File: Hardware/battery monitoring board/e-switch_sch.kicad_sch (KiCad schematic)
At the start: 8 parts, among them Q2 NMOS, Q3 PMOS, Q4 PMOS

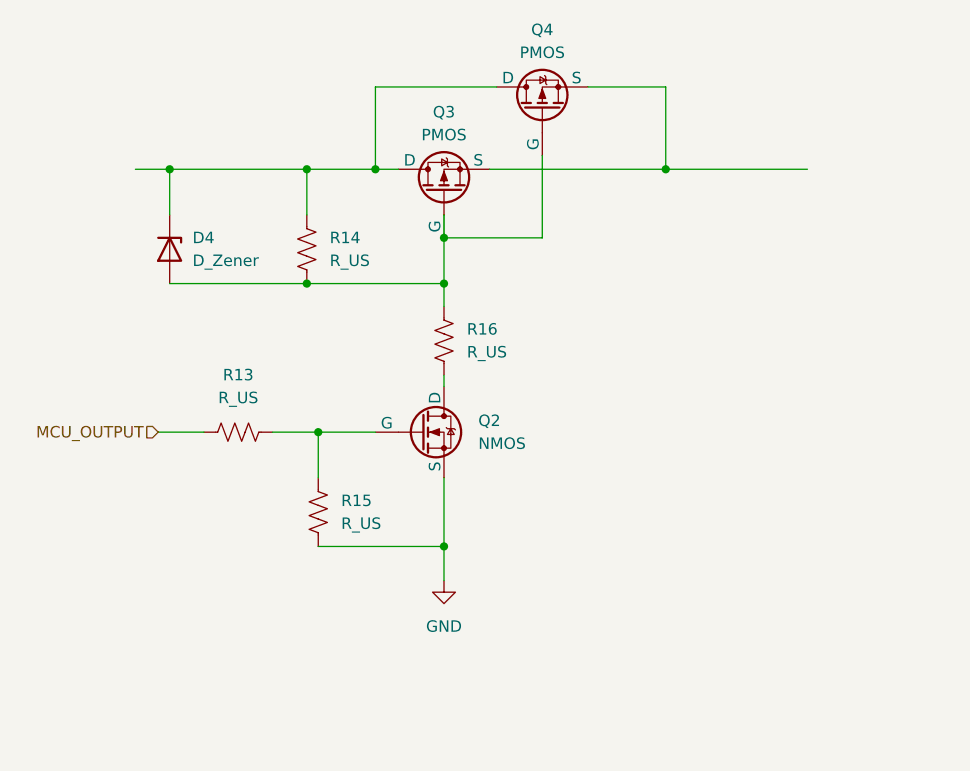
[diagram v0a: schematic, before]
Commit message: Added relay circuit
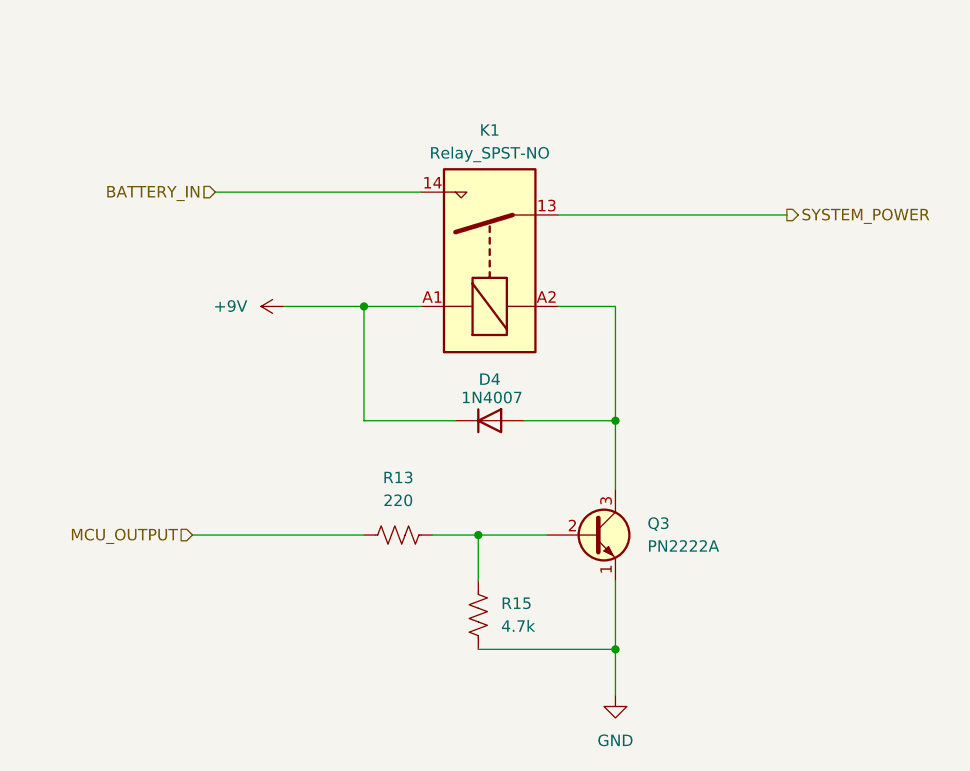
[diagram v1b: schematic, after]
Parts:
- removed D4: D_Zener, symbol Device:D_Zener
- removed Q2: NMOS, symbol Simulation_SPICE:NMOS
- removed Q3, Q4: PMOS, symbol Simulation_SPICE:PMOS
- removed R14, R16: R_US, symbol Device:R_US
- added D4: 1N4007, symbol Device:D
- added K1: Relay_SPST-NO, symbol Relay:Relay_SPST-NO
- added Q3: PN2222A, Package_TO_SOT_THT_AKL:TO-92_Inline_Wide_EBC, symbol PCM_Transistor_BJT_AKL:PN2222A
- R13: value R_US -> 220
- R15: value R_US -> 4.7k
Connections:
- net GND: now also Q3.1 (E)
- net at R13.2, R15.1: now also Q3.2 (B)
- new net: D4.2 (A), K1.A2, Q3.3 (C)
- new net +9V: D4.1 (K), K1.A1
- new net BATTERY_IN: K1.14
- new net SYSTEM_POWER: K1.13
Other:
- moved on the sheet: R13, R15

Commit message: Updated reference labels
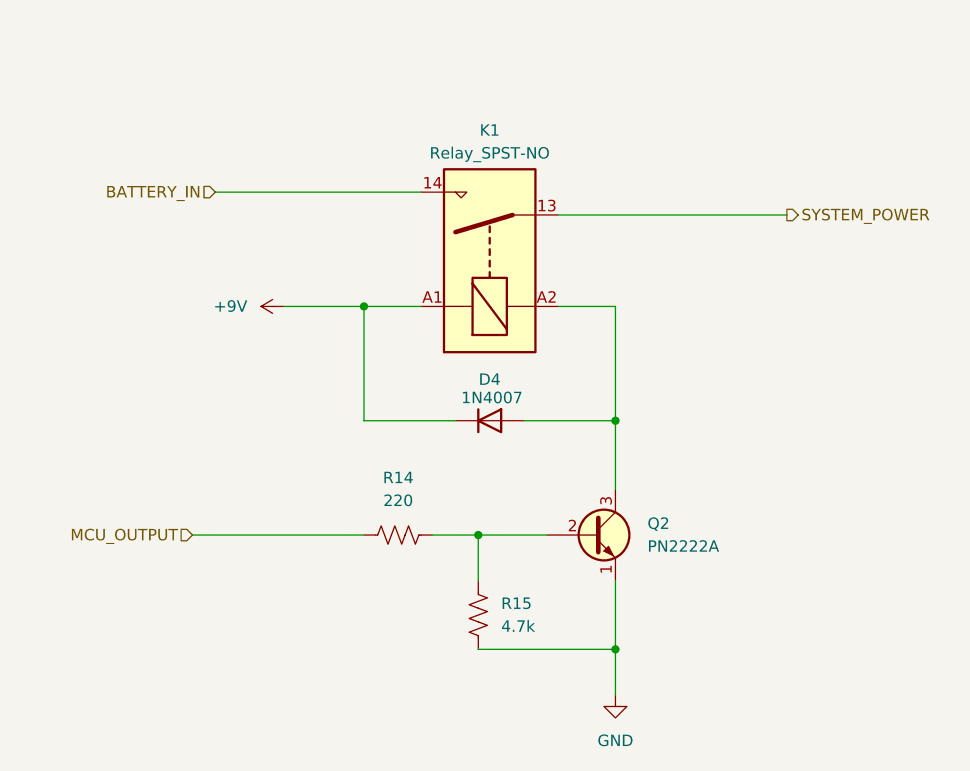
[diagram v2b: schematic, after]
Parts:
- renumbered Q3 to Q2, R13 to R14
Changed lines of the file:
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@@
   (symbol (lib_id "power:GND") (at 86.36 88.9 0) (unit 1)
     (in_bom yes) (on_board yes) (dnp no) (fields_autoplaced)
-    (property "Reference" "#PWR018" (at 86.36 95.25 0)
+    (property "Reference" "#PWR023" (at 86.36 95.25 0)
       (effects (font (size 1.27 1.27)) hide)
     )
@@
       (project "battery monitoring board"
         (path "/bf623d80-ca5a-491f-9daa-4dffbeba5279/d1e89632-1041-42ed-815d-03472eda859a"
-          (reference "#PWR018") (unit 1)
+          (reference "#PWR023") (unit 1)
         )
       )
@@
   (symbol (lib_id "PCM_Transistor_BJT_AKL:PN2222A") (at 83.82 71.12 0) (unit 1)
     (in_bom yes) (on_board yes) (dnp no) (fields_autoplaced)
-    (property "Reference" "Q3" (at 89.916 69.85 0)
+    (property "Reference" "Q2" (at 89.916 69.85 0)
       (effects (font (size 1.27 1.27)) (justify left))
     )
@@
       (project "battery monitoring board"
         (path "/bf623d80-ca5a-491f-9daa-4dffbeba5279/d1e89632-1041-42ed-815d-03472eda859a"
-          (reference "Q3") (unit 1)
+          (reference "Q2") (unit 1)
         )
       )
@@
   (symbol (lib_id "Device:R_US") (at 62.23 71.12 90) (unit 1)
     (in_bom yes) (on_board yes) (dnp no) (fields_autoplaced)
-    (property "Reference" "R13" (at 62.23 64.77 90)
+    (property "Reference" "R14" (at 62.23 64.77 90)
       (effects (font (size 1.27 1.27)))
     )
@@
       (project "battery monitoring board"
         (path "/bf623d80-ca5a-491f-9daa-4dffbeba5279/d1e89632-1041-42ed-815d-03472eda859a"
-          (reference "R13") (unit 1)
+          (reference "R14") (unit 1)
         )
       )
@@
   (symbol (lib_id "PCM_4ms_Power-symbol:+9V") (at 49.53 45.72 90) (unit 1)
     (in_bom yes) (on_board yes) (dnp no) (fields_autoplaced)
-    (property "Reference" "#PWR024" (at 53.34 45.72 0)
+    (property "Reference" "#PWR022" (at 53.34 45.72 0)
       (effects (font (size 1.27 1.27)) hide)
     )
@@
       (project "battery monitoring board"
         (path "/bf623d80-ca5a-491f-9daa-4dffbeba5279/d1e89632-1041-42ed-815d-03472eda859a"
-          (reference "#PWR024") (unit 1)
+          (reference "#PWR022") (unit 1)
         )
       )

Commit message: Revert "Updated reference labels"
This reverts commit 7ccd23260c988ead49c0bcfa936e50f6d09a7000.
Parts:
- renumbered Q2 to Q3, R14 to R13
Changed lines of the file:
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@@
   (symbol (lib_id "power:GND") (at 86.36 88.9 0) (unit 1)
     (in_bom yes) (on_board yes) (dnp no) (fields_autoplaced)
-    (property "Reference" "#PWR023" (at 86.36 95.25 0)
+    (property "Reference" "#PWR018" (at 86.36 95.25 0)
       (effects (font (size 1.27 1.27)) hide)
     )
@@
       (project "battery monitoring board"
         (path "/bf623d80-ca5a-491f-9daa-4dffbeba5279/d1e89632-1041-42ed-815d-03472eda859a"
-          (reference "#PWR023") (unit 1)
+          (reference "#PWR018") (unit 1)
         )
       )
@@
   (symbol (lib_id "PCM_Transistor_BJT_AKL:PN2222A") (at 83.82 71.12 0) (unit 1)
     (in_bom yes) (on_board yes) (dnp no) (fields_autoplaced)
-    (property "Reference" "Q2" (at 89.916 69.85 0)
+    (property "Reference" "Q3" (at 89.916 69.85 0)
       (effects (font (size 1.27 1.27)) (justify left))
     )
@@
       (project "battery monitoring board"
         (path "/bf623d80-ca5a-491f-9daa-4dffbeba5279/d1e89632-1041-42ed-815d-03472eda859a"
-          (reference "Q2") (unit 1)
+          (reference "Q3") (unit 1)
         )
       )
@@
   (symbol (lib_id "Device:R_US") (at 62.23 71.12 90) (unit 1)
     (in_bom yes) (on_board yes) (dnp no) (fields_autoplaced)
-    (property "Reference" "R14" (at 62.23 64.77 90)
+    (property "Reference" "R13" (at 62.23 64.77 90)
       (effects (font (size 1.27 1.27)))
     )
@@
       (project "battery monitoring board"
         (path "/bf623d80-ca5a-491f-9daa-4dffbeba5279/d1e89632-1041-42ed-815d-03472eda859a"
-          (reference "R14") (unit 1)
+          (reference "R13") (unit 1)
         )
       )
@@
   (symbol (lib_id "PCM_4ms_Power-symbol:+9V") (at 49.53 45.72 90) (unit 1)
     (in_bom yes) (on_board yes) (dnp no) (fields_autoplaced)
-    (property "Reference" "#PWR022" (at 53.34 45.72 0)
+    (property "Reference" "#PWR024" (at 53.34 45.72 0)
       (effects (font (size 1.27 1.27)) hide)
     )
@@
       (project "battery monitoring board"
         (path "/bf623d80-ca5a-491f-9daa-4dffbeba5279/d1e89632-1041-42ed-815d-03472eda859a"
-          (reference "#PWR022") (unit 1)
+          (reference "#PWR024") (unit 1)
         )
       )
